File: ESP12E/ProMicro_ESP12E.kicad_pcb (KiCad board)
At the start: 2 copper layers, 17.8 x 33 mm, 15 parts, among them J1 ESP01(Prog), J2 Conn_01x02, J3 LCD, J4 UART, Q1 mmbt2222, Q2 mmbt2222, U2 ESP-12E

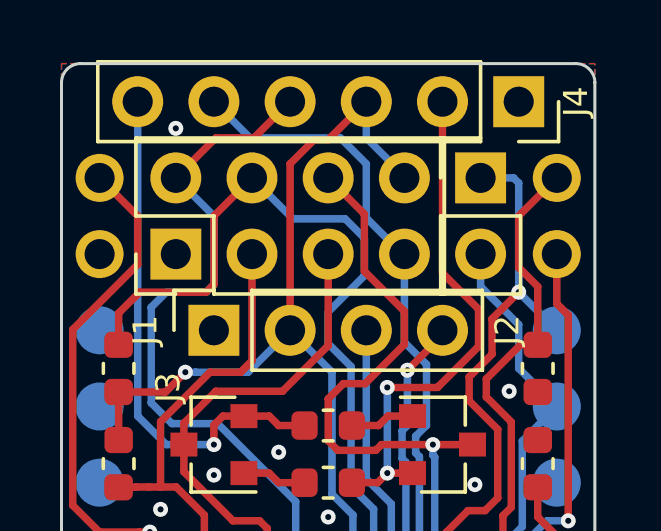
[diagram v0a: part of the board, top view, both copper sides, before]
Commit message: make controller holes wide enough
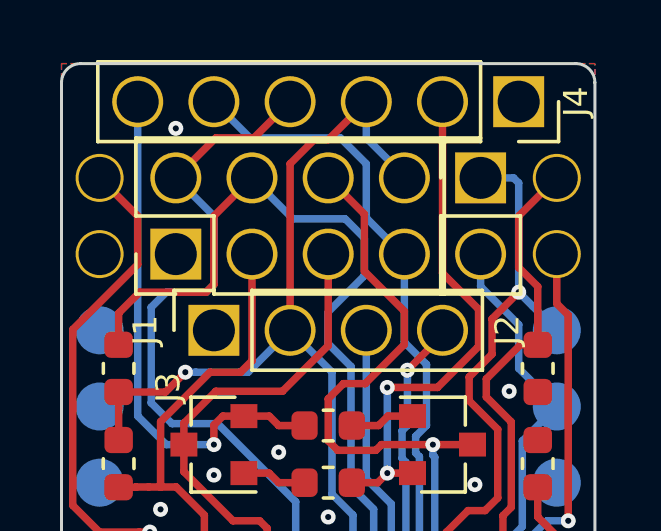
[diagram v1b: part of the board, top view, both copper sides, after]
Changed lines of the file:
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@@
     (mod_text_width 0.15)
     (pad_size 1.6 1.6)
-    (pad_drill 1)
+    (pad_drill 1.4)
     (pad_to_mask_clearance 0)
     (aux_axis_origin 57.15 116.84)
@@
     (pad 22 smd oval (at 15.24 -5.08) (size 1.6 1.6) (layers B.Cu B.Paste B.Mask)
       (net 2 Reset))
-    (pad 12 thru_hole oval (at 0 -27.94) (size 1.6 1.6) (drill 1) (layers *.Cu *.Mask)
+    (pad 12 thru_hole circle (at 0 -27.94) (size 1.6 1.6) (drill 1.4) (layers *.Cu *.Mask)
       (net 13 D9))
     (pad 21 smd oval (at 15.24 -7.62) (size 1.6 1.6) (layers B.Cu B.Paste B.Mask)
       (net 3 +3V3))
-    (pad 11 thru_hole oval (at 0 -25.4) (size 1.6 1.6) (drill 1) (layers *.Cu *.Mask))
+    (pad 11 thru_hole circle (at 0 -25.4) (size 1.6 1.6) (drill 1.4) (layers *.Cu *.Mask))
     (pad 20 smd oval (at 15.24 -10.16) (size 1.6 1.6) (layers B.Cu B.Paste B.Mask))
     (pad 10 smd oval (at 0 -22.86) (size 1.6 1.6) (layers B.Cu B.Paste B.Mask))
@@
     (pad 5 smd oval (at 0 -10.16) (size 1.6 1.6) (layers B.Cu B.Paste B.Mask)
       (net 12 SDA))
-    (pad 14 thru_hole oval (at 15.24 -25.4) (size 1.6 1.6) (drill 1) (layers *.Cu *.Mask)
+    (pad 14 thru_hole circle (at 15.24 -25.4) (size 1.6 1.6) (drill 1.4) (layers *.Cu *.Mask)
       (net 7 MOSI))
     (pad 4 smd oval (at 0 -7.62) (size 1.6 1.6) (layers B.Cu B.Paste B.Mask)
       (net 1 GND))
-    (pad 13 thru_hole oval (at 15.24 -27.94) (size 1.6 1.6) (drill 1) (layers *.Cu *.Mask)
+    (pad 13 thru_hole circle (at 15.24 -27.94) (size 1.6 1.6) (drill 1.4) (layers *.Cu *.Mask)
       (net 8 D10))
     (pad 3 smd oval (at 0 -5.08) (size 1.6 1.6) (layers B.Cu B.Paste B.Mask))
@@
     (fp_line (start 0.635 -1.27) (end 1.27 -0.635) (layer F.Fab) (width 0.1))
     (fp_line (start -1.27 -1.27) (end 0.635 -1.27) (layer F.Fab) (width 0.1))
-    (pad 6 thru_hole oval (at 0 12.7 270) (size 1.7 1.7) (drill 1) (layers *.Cu *.Mask)
+    (pad 6 thru_hole circle (at 0 12.7 270) (size 1.7 1.7) (drill 1.4) (layers *.Cu *.Mask)
       (net 17 /~DTR))
-    (pad 5 thru_hole oval (at 0 10.16 270) (size 1.7 1.7) (drill 1) (layers *.Cu *.Mask)
+    (pad 5 thru_hole circle (at 0 10.16 270) (size 1.7 1.7) (drill 1.4) (layers *.Cu *.Mask)
       (net 9 RXD))
-    (pad 4 thru_hole oval (at 0 7.62 270) (size 1.7 1.7) (drill 1) (layers *.Cu *.Mask)
+    (pad 4 thru_hole circle (at 0 7.62 270) (size 1.7 1.7) (drill 1.4) (layers *.Cu *.Mask)
       (net 10 TXD))
-    (pad 3 thru_hole oval (at 0 5.08 270) (size 1.7 1.7) (drill 1) (layers *.Cu *.Mask)
+    (pad 3 thru_hole circle (at 0 5.08 270) (size 1.7 1.7) (drill 1.4) (layers *.Cu *.Mask)
       (net 3 +3V3))
-    (pad 2 thru_hole oval (at 0 2.54 270) (size 1.7 1.7) (drill 1) (layers *.Cu *.Mask)
+    (pad 2 thru_hole circle (at 0 2.54 270) (size 1.7 1.7) (drill 1.4) (layers *.Cu *.Mask)
       (net 18 /~RTS))
-    (pad 1 thru_hole rect (at 0 0 270) (size 1.7 1.7) (drill 1) (layers *.Cu *.Mask)
+    (pad 1 thru_hole rect (at 0 0 270) (size 1.7 1.7) (drill 1.4) (layers *.Cu *.Mask)
       (net 1 GND))
   )
@@
     (fp_line (start 1.27 -1.27) (end 1.27 3.81) (layer F.Fab) (width 0.1))
     (fp_line (start -0.635 -1.27) (end 1.27 -1.27) (layer F.Fab) (width 0.1))
-    (pad 2 thru_hole oval (at 0 2.54) (size 1.7 1.7) (drill 1) (layers *.Cu *.Mask)
+    (pad 2 thru_hole circle (at 0 2.54) (size 1.7 1.7) (drill 1.4) (layers *.Cu *.Mask)
       (net 5 SCK))
-    (pad 1 thru_hole rect (at 0 0) (size 1.7 1.7) (drill 1) (layers *.Cu *.Mask)
+    (pad 1 thru_hole rect (at 0 0) (size 1.7 1.7) (drill 1.4) (layers *.Cu *.Mask)
       (net 6 MISO))
   )
@@
     (fp_line (start 0.635 -1.27) (end 1.27 -0.635) (layer F.Fab) (width 0.1))
     (fp_line (start -1.27 -1.27) (end 0.635 -1.27) (layer F.Fab) (width 0.1))
-    (pad 4 thru_hole oval (at 0 7.62 90) (size 1.7 1.7) (drill 1) (layers *.Cu *.Mask)
+    (pad 4 thru_hole circle (at 0 7.62 90) (size 1.7 1.7) (drill 1.4) (layers *.Cu *.Mask)
       (net 12 SDA))
-    (pad 3 thru_hole oval (at 0 5.08 90) (size 1.7 1.7) (drill 1) (layers *.Cu *.Mask)
+    (pad 3 thru_hole circle (at 0 5.08 90) (size 1.7 1.7) (drill 1.4) (layers *.Cu *.Mask)
       (net 11 SCL))
-    (pad 2 thru_hole oval (at 0 2.54 90) (size 1.7 1.7) (drill 1) (layers *.Cu *.Mask)
+    (pad 2 thru_hole circle (at 0 2.54 90) (size 1.7 1.7) (drill 1.4) (layers *.Cu *.Mask)
       (net 3 +3V3))
-    (pad 1 thru_hole rect (at 0 0 90) (size 1.7 1.7) (drill 1) (layers *.Cu *.Mask)
+    (pad 1 thru_hole rect (at 0 0 90) (size 1.7 1.7) (drill 1.4) (layers *.Cu *.Mask)
       (net 1 GND))
   )
@@
     (fp_line (start 3.81 -1.27) (end 3.81 8.89) (layer F.Fab) (width 0.1))
     (fp_line (start 0 -1.27) (end 3.81 -1.27) (layer F.Fab) (width 0.1))
-    (pad 8 thru_hole oval (at 2.54 7.62 90) (size 1.7 1.7) (drill 1) (layers *.Cu *.Mask)
+    (pad 8 thru_hole circle (at 2.54 7.62 90) (size 1.7 1.7) (drill 1.4) (layers *.Cu *.Mask)
       (net 3 +3V3))
-    (pad 7 thru_hole oval (at 0 7.62 90) (size 1.7 1.7) (drill 1) (layers *.Cu *.Mask)
+    (pad 7 thru_hole circle (at 0 7.62 90) (size 1.7 1.7) (drill 1.4) (layers *.Cu *.Mask)
       (net 9 RXD))
-    (pad 6 thru_hole oval (at 2.54 5.08 90) (size 1.7 1.7) (drill 1) (layers *.Cu *.Mask)
+    (pad 6 thru_hole circle (at 2.54 5.08 90) (size 1.7 1.7) (drill 1.4) (layers *.Cu *.Mask)
       (net 2 Reset))
-    (pad 5 thru_hole oval (at 0 5.08 90) (size 1.7 1.7) (drill 1) (layers *.Cu *.Mask)
+    (pad 5 thru_hole circle (at 0 5.08 90) (size 1.7 1.7) (drill 1.4) (layers *.Cu *.Mask)
       (net 14 GPIO0))
-    (pad 4 thru_hole oval (at 2.54 2.54 90) (size 1.7 1.7) (drill 1) (layers *.Cu *.Mask)
+    (pad 4 thru_hole circle (at 2.54 2.54 90) (size 1.7 1.7) (drill 1.4) (layers *.Cu *.Mask)
       (net 16 /EN))
-    (pad 3 thru_hole oval (at 0 2.54 90) (size 1.7 1.7) (drill 1) (layers *.Cu *.Mask)
+    (pad 3 thru_hole circle (at 0 2.54 90) (size 1.7 1.7) (drill 1.4) (layers *.Cu *.Mask)
       (net 15 GPIO2))
-    (pad 2 thru_hole oval (at 2.54 0 90) (size 1.7 1.7) (drill 1) (layers *.Cu *.Mask)
+    (pad 2 thru_hole circle (at 2.54 0 90) (size 1.7 1.7) (drill 1.4) (layers *.Cu *.Mask)
       (net 10 TXD))
-    (pad 1 thru_hole rect (at 0 0 90) (size 1.7 1.7) (drill 1) (layers *.Cu *.Mask)
+    (pad 1 thru_hole rect (at 0 0 90) (size 1.7 1.7) (drill 1.4) (layers *.Cu *.Mask)
       (net 1 GND))
   )
